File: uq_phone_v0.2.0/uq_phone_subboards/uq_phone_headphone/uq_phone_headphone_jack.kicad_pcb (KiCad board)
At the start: 2 copper layers, 9.2 x 14.2 mm, 6 parts

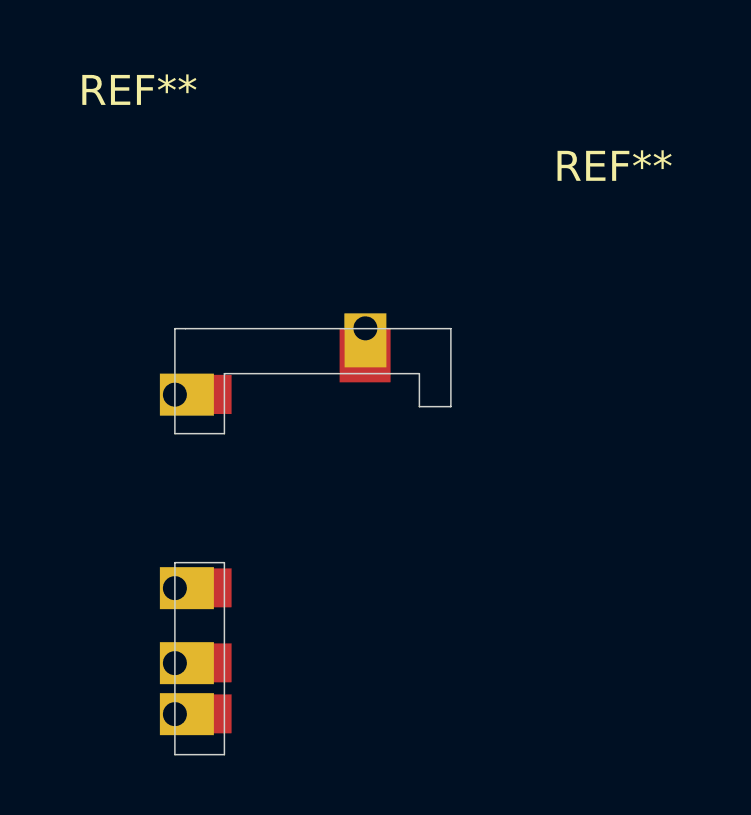
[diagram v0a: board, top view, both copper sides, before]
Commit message: Prototype without GPIO expander
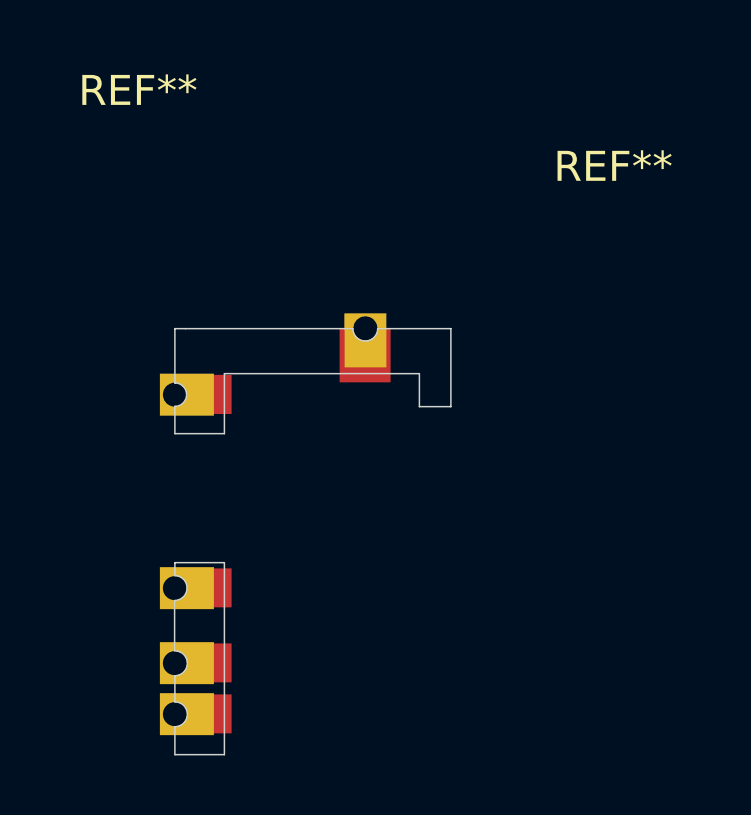
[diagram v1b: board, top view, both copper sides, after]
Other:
- outline, holes or cut-outs redrawn
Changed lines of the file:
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@@
 			(outputformat 1)
 			(mirror no)
-			(drillshape 1)
+			(drillshape 0)
 			(scaleselection 1)
-			(outputdirectory "")
+			(outputdirectory "Gerber/")
 		)
 	)
@@
 	)
 	(gr_line
+		(start 142.25 81.6425)
+		(end 142.25 80.77)
+		(stroke
+			(width 0.05)
+			(type default)
+		)
+		(layer "Edge.Cuts")
+	)
+	(gr_line
 		(start 143.9 83.4)
 		(end 143.9 77)
@@
 	(gr_line
 		(start 142.25 83.4)
-		(end 142.25 77)
+		(end 142.25 82.47)
+		(stroke
+			(width 0.05)
+			(type default)
+		)
+		(layer "Edge.Cuts")
+	)
+	(gr_arc
+		(start 142.25 71.01)
+		(mid 142.64 71.4)
+		(end 142.25 71.79)
+		(stroke
+			(width 0.05)
+			(type solid)
+		)
+		(layer "Edge.Cuts")
+	)
+	(gr_line
+		(start 142.25 77)
+		(end 142.25 77.43)
 		(stroke
 			(width 0.05)
@@
 	)
 	(gr_line
+		(start 151.45 69.2)
+		(end 149.01 69.2)
+		(stroke
+			(width 0.05)
+			(type default)
+		)
+		(layer "Edge.Cuts")
+	)
+	(gr_line
 		(start 151.45 71.8)
 		(end 150.4 71.8)
@@
 		(layer "Edge.Cuts")
 	)
+	(gr_arc
+		(start 142.25 77.430121)
+		(mid 142.654969 77.85)
+		(end 142.24 78.26)
+		(stroke
+			(width 0.05)
+			(type default)
+		)
+		(layer "Edge.Cuts")
+	)
 	(gr_line
 		(start 142.6 69.2)
-		(end 151.45 69.2)
-		(stroke
-			(width 0.05)
-			(type default)
-		)
-		(layer "Edge.Cuts")
-	)
-	(gr_line
-		(start 142.25 72.7)
+		(end 148.18 69.2)
+		(stroke
+			(width 0.05)
+			(type default)
+		)
+		(layer "Edge.Cuts")
+	)
+	(gr_line
+		(start 142.25 71.79)
+		(end 142.25 72.7)
+		(stroke
+			(width 0.05)
+			(type default)
+		)
+		(layer "Edge.Cuts")
+	)
+	(gr_line
+		(start 142.25 71.01)
 		(end 142.25 69.2)
 		(stroke
@@
 		(stroke
 			(width 0.05)
+			(type default)
+		)
+		(layer "Edge.Cuts")
+	)
+	(gr_arc
+		(start 142.25 81.64)
+		(mid 142.665 82.055)
+		(end 142.25 82.47)
+		(stroke
+			(width 0.05)
+			(type default)
+		)
+		(layer "Edge.Cuts")
+	)
+	(gr_line
+		(start 142.24 79.9325)
+		(end 142.24 78.27)
+		(stroke
+			(width 0.05)
+			(type default)
+		)
+		(layer "Edge.Cuts")
+	)
+	(gr_arc
+		(start 142.25 79.94)
+		(mid 142.665 80.355)
+		(end 142.25 80.77)
+		(stroke
+			(width 0.05)
+			(type default)
+		)
+		(layer "Edge.Cuts")
+	)
+	(gr_arc
+		(start 149.01 69.199867)
+		(mid 148.595066 69.614868)
+		(end 148.18 69.2)
+		(stroke
+			(width 0.05)
